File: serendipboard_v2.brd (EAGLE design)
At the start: 34.3 x 48.3 mm, 85 parts, among them IC1 TP4056, IC2 DW01A, IC3 DS3231/SO, J4 USB3076-XX-X_REVC, Q1 FS8205A, Q2 MMBT2222ALT1G, Q3 RUC002N05HZGT116, Q4 DMG3415U, Q5 MMBT2222ALT1G, Q7 RUC002N05HZGT116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

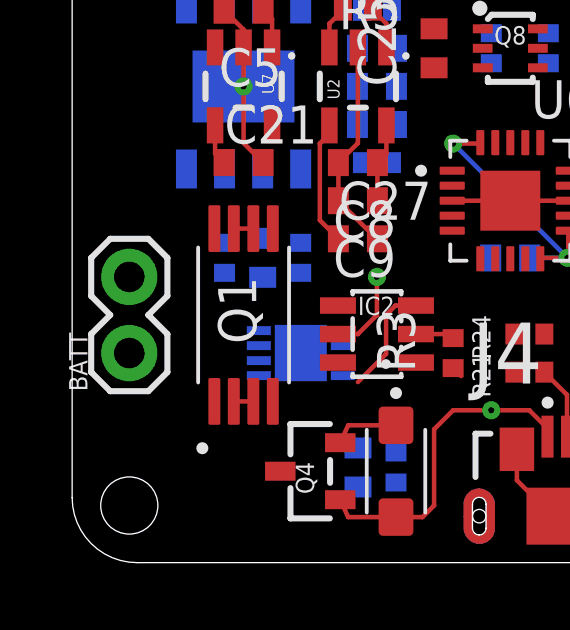
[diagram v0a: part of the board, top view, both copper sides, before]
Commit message: Update serendipboard_v2.brd
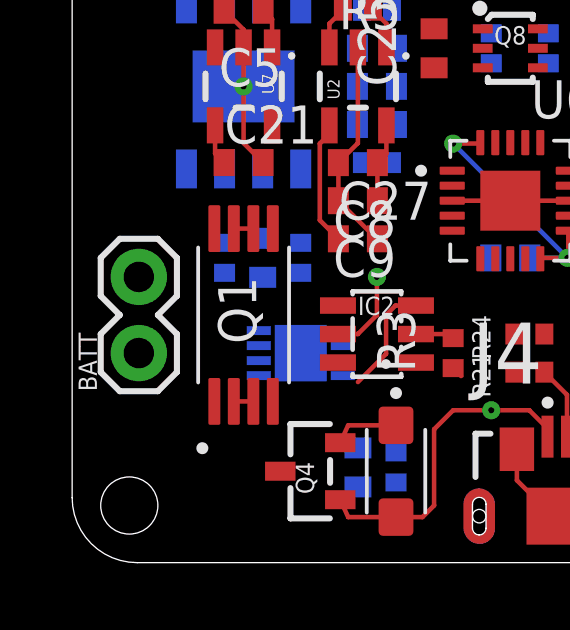
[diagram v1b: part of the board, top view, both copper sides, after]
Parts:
- moved BATT 0.32 mm to (2.22, 6.99)
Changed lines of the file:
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@@
 <attribute name="WEBLINK" value="https://www.mouser.com/ProductDetail/Microchip-Technology-Micrel/MIC5219-33YM5-TR?qs=U6T8BxXiZAWojkIJMtSJlw%3D%3D" x="-80.645" y="113.665" size="1.778" layer="27" rot="R180" display="off"/>
 </element>
-<element name="BATT" library="SparkFun-Connectors" package="1X02" value="" x="1.905" y="6.985" smashed="yes" rot="R90">
-<attribute name="NAME" x="0.508" y="5.715" size="0.6096" layer="25" font="vector" ratio="20" rot="R90"/>
-<attribute name="VALUE" x="3.937" y="5.715" size="0.6096" layer="27" font="vector" ratio="20" rot="R90"/>
+<element name="BATT" library="SparkFun-Connectors" package="1X02" value="" x="2.2225" y="6.985" smashed="yes" rot="R90">
+<attribute name="NAME" x="0.8255" y="5.715" size="0.6096" layer="25" font="vector" ratio="20" rot="R90"/>
+<attribute name="VALUE" x="4.2545" y="5.715" size="0.6096" layer="27" font="vector" ratio="20" rot="R90"/>
 </element>
 </elements>
@@
 <wire x1="6.04" y1="5.375" x2="5.39" y2="5.375" width="0.1524" layer="1"/>
 <contactref element="BATT" pad="1"/>
-<wire x1="1.905" y1="6.985" x2="5.39" y2="5.375" width="0" layer="19" extent="1-1"/>
+<wire x1="2.2225" y1="6.985" x2="5.39" y2="5.375" width="0" layer="19" extent="1-1"/>
 </signal>
 <signal name="N$4">
@@
 <wire x1="7.62" y1="13.125" x2="9.66" y2="13.335" width="0" layer="19" extent="16-16"/>
 <wire x1="5.08" y1="10.66" x2="7.62" y2="13.125" width="0" layer="19" extent="16-16"/>
-<wire x1="1.905" y1="9.525" x2="5.08" y2="10.66" width="0" layer="19" extent="16-16"/>
+<wire x1="2.2225" y1="9.525" x2="5.08" y2="10.66" width="0" layer="19" extent="16-16"/>
 <wire x1="6.9375" y1="3.048" x2="5.08" y2="10.66" width="0" layer="19" extent="1-16"/>
 </signal>

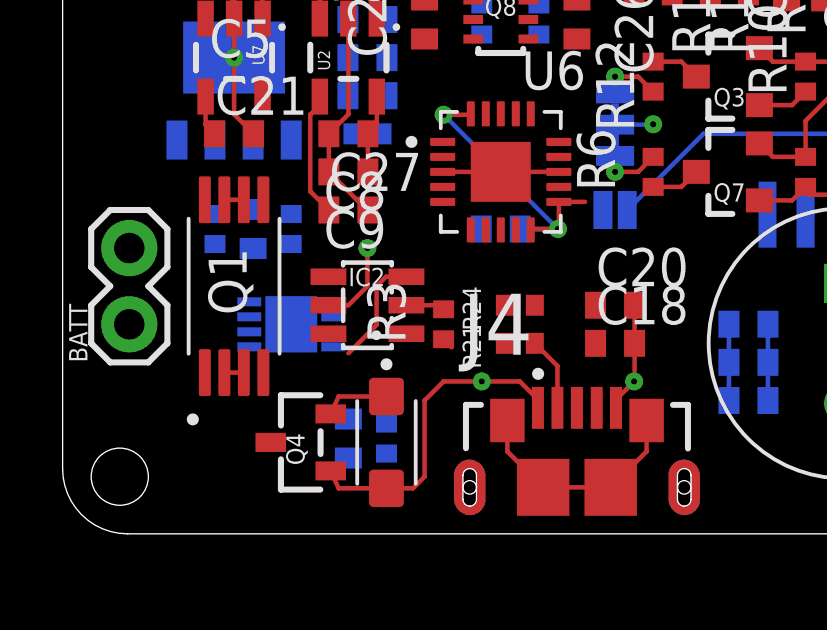
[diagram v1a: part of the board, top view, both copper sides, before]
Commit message: Update serendipboard_v2.brd
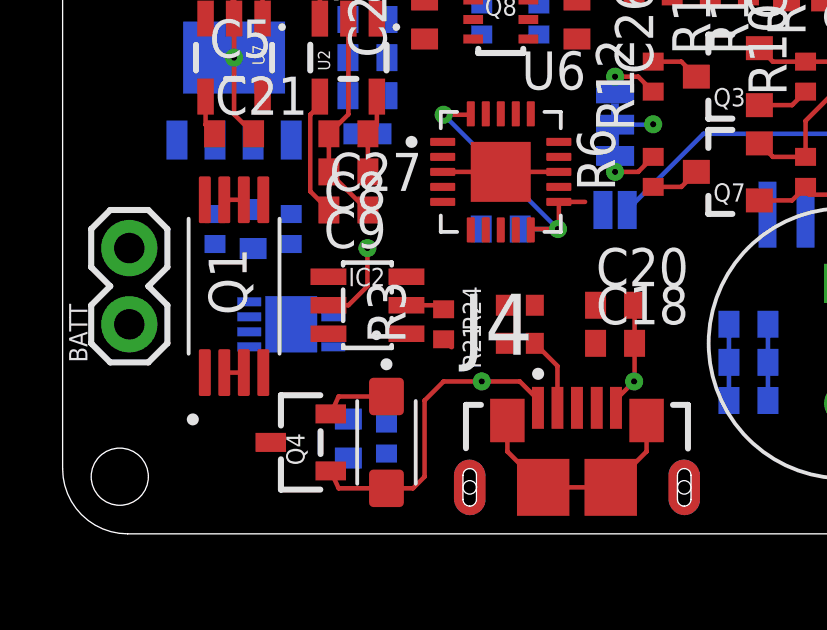
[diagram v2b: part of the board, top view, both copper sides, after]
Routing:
- net N$2: track 3.75 -> 0.00 mm
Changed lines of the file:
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@@
 <contactref element="Q1" pad="5"/>
 <contactref element="IC2" pad="3"/>
-<wire x1="9.525" y1="6.0198" x2="10.4648" y2="6.9596" width="0.1524" layer="1"/>
-<wire x1="10.4648" y1="6.9596" x2="10.4648" y2="8.255" width="0.1524" layer="1"/>
-<wire x1="10.4648" y1="8.255" x2="10.7798" y2="8.57" width="0.1524" layer="1"/>
-<wire x1="10.7798" y1="8.57" x2="11.46" y2="8.57" width="0.1524" layer="1"/>
-<wire x1="11.46" y1="8.57" x2="6.69" y2="11.135" width="0" layer="19" extent="1-1"/>
+<wire x1="6.69" y1="11.135" x2="11.46" y2="8.57" width="0" layer="19" extent="1-1"/>
 </signal>
 <signal name="N$5">

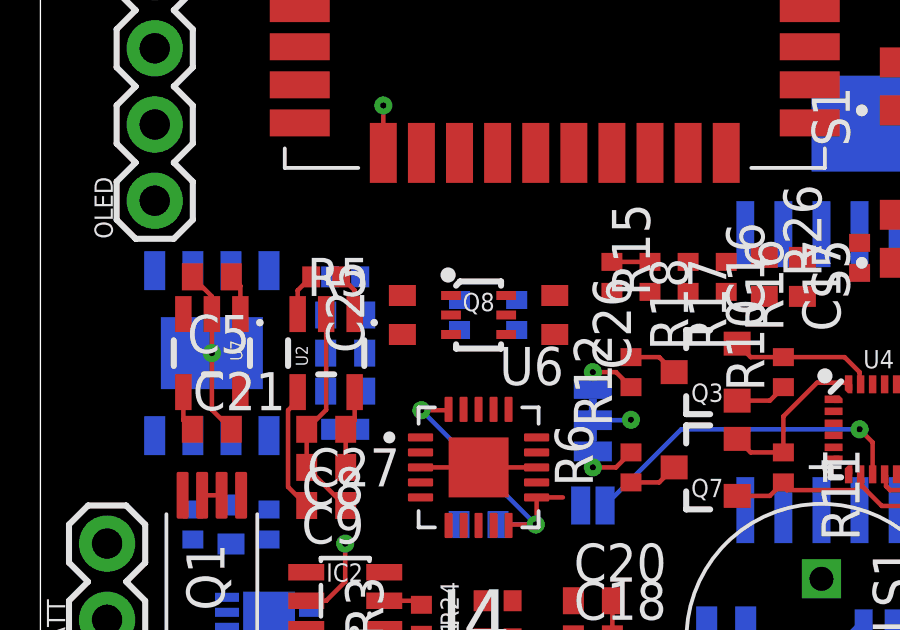
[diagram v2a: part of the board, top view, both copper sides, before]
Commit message: Update serendipboard_v2.brd
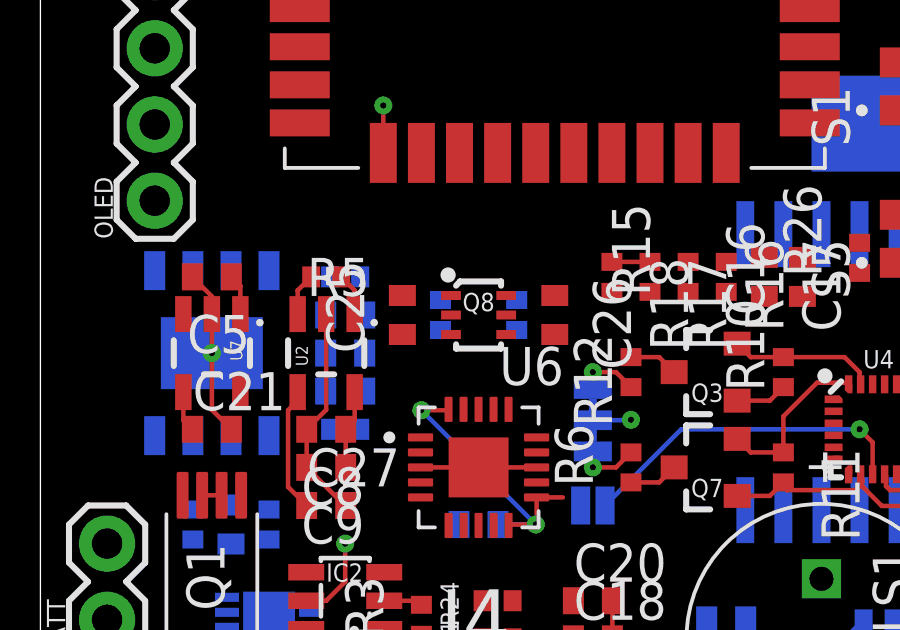
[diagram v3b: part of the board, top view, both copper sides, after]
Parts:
- moved R23 0.63 mm to (13.3, 17.1)
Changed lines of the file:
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@@
 </layers>
 <board>
-<fusionsync huburn="a.YnVzaW5lc3M6aG90bWFpbDIyNTY5Mg" projecturn="a.YnVzaW5lc3M6aG90bWFpbDIyNTY5MiNEMjAyMTAyMjYzODcwODA0ODE" f3durn="urn:adsk.wipprod:dm.lineage:5p1CPkeoRTeQBctxtFipzA" pcbguid="" lastpulledtime="" lastsyncedchangeguid="" latestrevisionid="0848454d-5bbb-43fb-8d8e-27c1f2ded824" lastsyncedrevisionid="0848454d-5bbb-43fb-8d8e-27c1f2ded824" lastboardhashguid="b401df1f-909b-11eb-b8ce-9c009d1c97d0" lastpushedtime="2021-03-17T16:29:33Z" linktopcb3d="false"/>
+<fusionsync huburn="a.YnVzaW5lc3M6aG90bWFpbDIyNTY5Mg" projecturn="a.YnVzaW5lc3M6aG90bWFpbDIyNTY5MiNEMjAyMTAyMjYzODcwODA0ODE" f3durn="urn:adsk.wipprod:dm.lineage:5p1CPkeoRTeQBctxtFipzA" pcbguid="" lastpulledtime="" lastsyncedchangeguid="" latestrevisionid="0848454d-5bbb-43fb-8d8e-27c1f2ded824" lastsyncedrevisionid="0848454d-5bbb-43fb-8d8e-27c1f2ded824" lastboardhashguid="b401df1f-909b-11eb-b8ce-9c009d1c97d0" lastpushedtime="2021-03-17T16:29:33Z" linktopcb3d="true"/>
 <fusionteam huburn="a.YnVzaW5lc3M6aG90bWFpbDIyNTY5Mg" projecturn="a.YnVzaW5lc3M6aG90bWFpbDIyNTY5MiNEMjAyMTAyMjYzODcwODA0ODE" folderUrn="urn:adsk.wipprod:fs.folder:co.dUA13uBtTS2Ov44EvO0svw" urn="urn:adsk.wipprod:dm.lineage:Zp6-x7SYSPeZgPEikwpQaw"  versionUrn="urn:adsk.wipprod:fs.file:vf.Zp6-x7SYSPeZgPEikwpQaw?version=1" camFileUrn="" camFileVersionUrn="" lastpublishedchangeguid="f1674931-6e59-d979-c39e-c9ae2950564c"/>
 <plain>
@@
 <attribute name="VALUE" x="18.415" y="17.78" size="1.27" layer="28" rot="MR270"/>
 </element>
-<element name="R23" library="rcl" library_urn="urn:adsk.eagle:library:334" package="R0402" package3d_urn="urn:adsk.eagle:package:23547/3" value="10k" x="13.97" y="17.145" smashed="yes" rot="MR270">
-<attribute name="NAME" x="12.7" y="19.05" size="1.27" layer="26" rot="MR90"/>
-<attribute name="POPULARITY" value="34" x="105.41" y="-5.715" size="1.778" layer="28" rot="MR270" display="off"/>
-<attribute name="SPICEPREFIX" value="R" x="105.41" y="-5.715" size="1.778" layer="28" rot="MR270" display="off"/>
-<attribute name="VALUE" x="16.51" y="17.78" size="1.27" layer="28" rot="MR270"/>
+<element name="R23" library="rcl" library_urn="urn:adsk.eagle:library:334" package="R0402" package3d_urn="urn:adsk.eagle:package:23547/3" value="10k" x="13.335" y="17.145" smashed="yes" rot="MR270">
+<attribute name="NAME" x="12.065" y="19.05" size="1.27" layer="26" rot="MR90"/>
+<attribute name="POPULARITY" value="34" x="104.775" y="-5.715" size="1.778" layer="28" rot="MR270" display="off"/>
+<attribute name="SPICEPREFIX" value="R" x="104.775" y="-5.715" size="1.778" layer="28" rot="MR270" display="off"/>
+<attribute name="VALUE" x="15.875" y="17.78" size="1.27" layer="28" rot="MR270"/>
 </element>
 <element name="R24" library="rcl" library_urn="urn:adsk.eagle:library:334" package="R0402" package3d_urn="urn:adsk.eagle:package:23547/3" value="27" x="15.24" y="7.62" smashed="yes" rot="R180">
@@
 <contactref element="R23" pad="2"/>
 <contactref element="Q8" pad="2"/>
-<wire x1="13.685" y1="17.145" x2="13.97" y2="16.645" width="0" layer="19" extent="1-16"/>
+<wire x1="13.685" y1="17.145" x2="13.335" y2="16.645" width="0" layer="19" extent="1-16"/>
 </signal>
 <signal name="EN">
@@
 <contactref element="Q8" pad="4"/>
 <contactref element="U6" pad="19"/>
-<wire x1="13.97" y1="17.645" x2="15.525" y2="16.495" width="0" layer="19" extent="1-16"/>
+<wire x1="13.335" y1="17.645" x2="15.525" y2="16.495" width="0" layer="19" extent="1-16"/>
 <wire x1="14.105" y1="14" x2="15.525" y2="16.495" width="0" layer="19" extent="1-1"/>
 </signal>

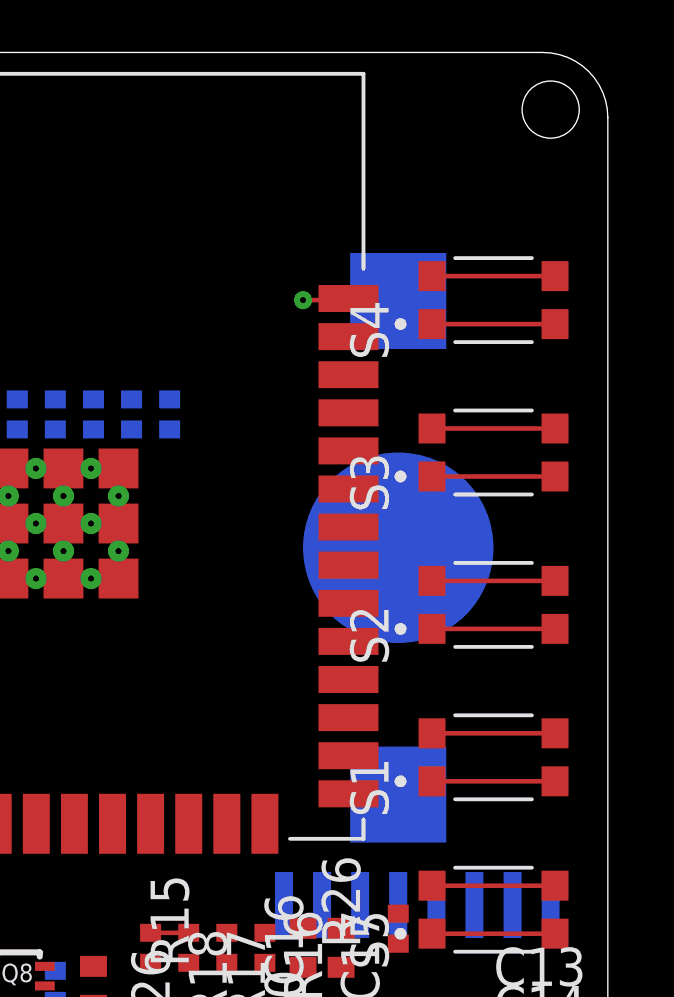
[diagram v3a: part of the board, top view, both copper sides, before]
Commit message: Update serendipboard_v2.brd
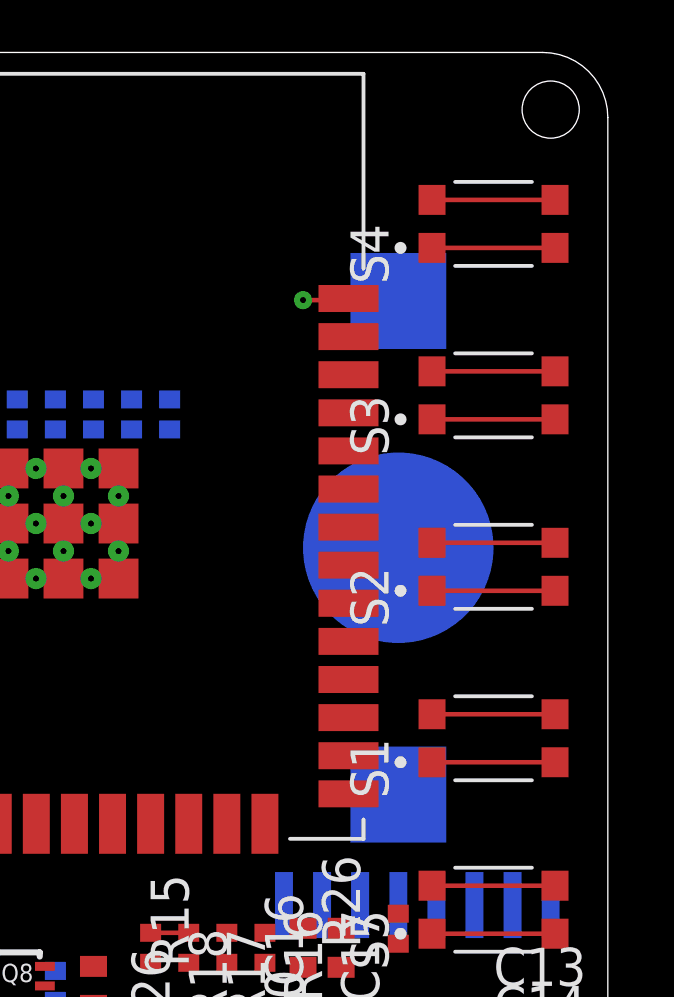
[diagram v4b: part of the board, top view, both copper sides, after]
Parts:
- moved S4 2.54 mm to (30.5, 42.5)
- moved S3 1.91 mm to (30.5, 36.8)
- moved S2 1.27 mm to (30.5, 31.1)
- moved S1 0.63 mm to (30.5, 25.4)

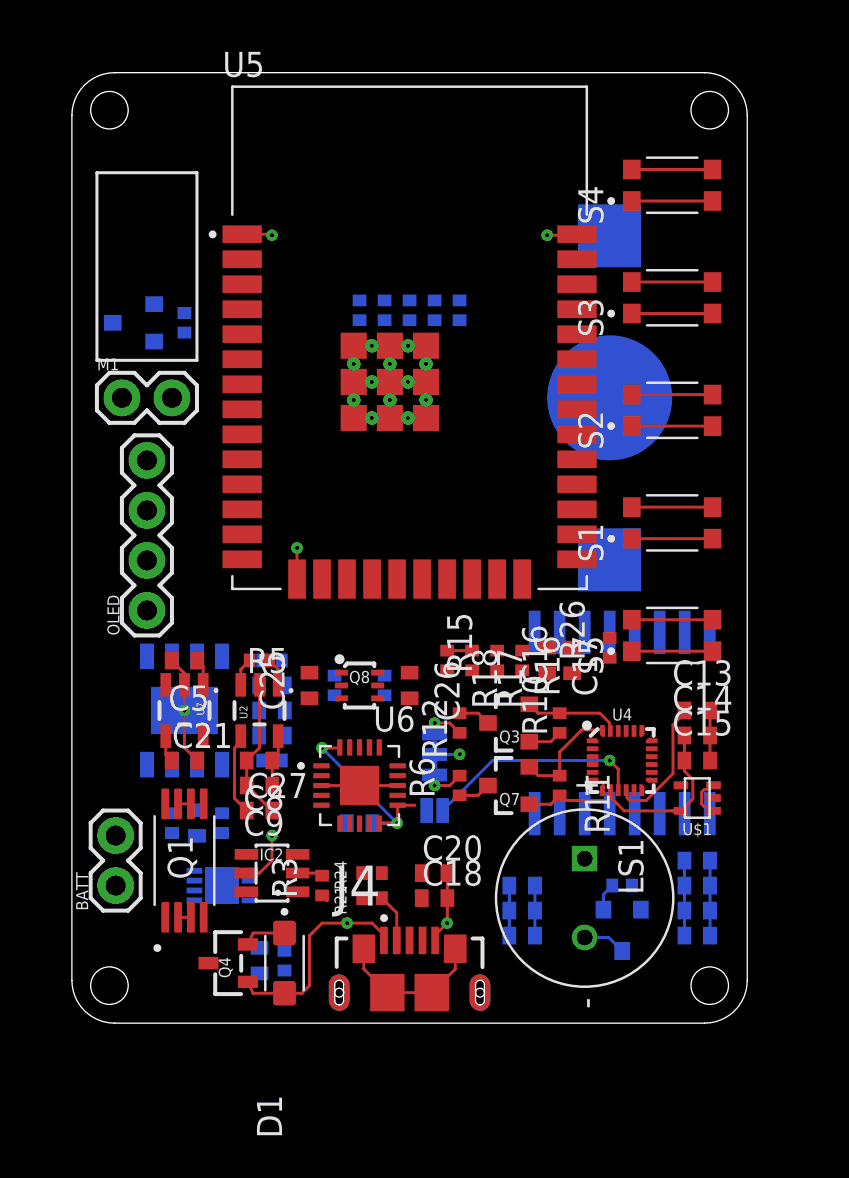
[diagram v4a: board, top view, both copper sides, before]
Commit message: Update serendipboard_v2.brd
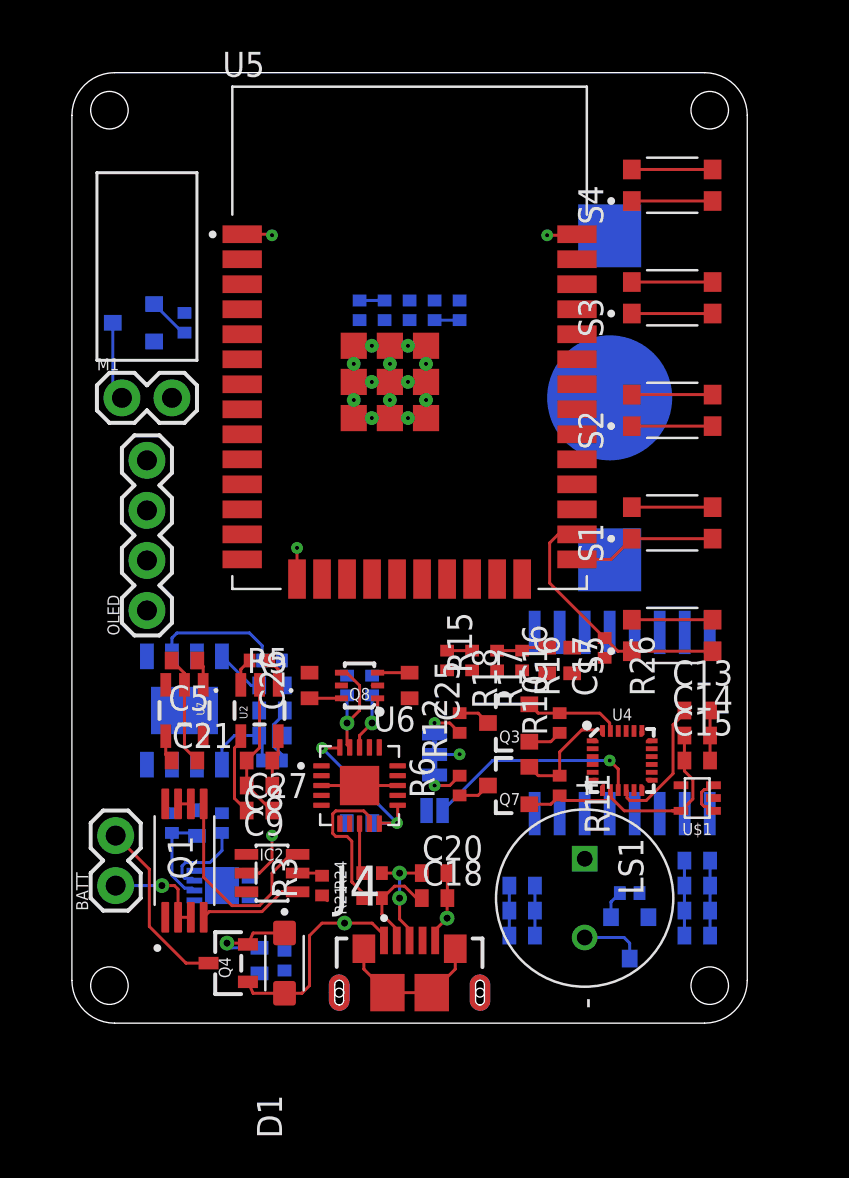
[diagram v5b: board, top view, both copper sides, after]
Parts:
- moved C25 5.08 mm to (17.1, 17.1), turned to 270 degrees
- moved C26 5.08 mm to (12.1, 17.1), turned to 90 degrees
- moved R22 0.63 mm to (15.2, 17.1)
- moved R23 0.63 mm to (14.0, 17.1), turned to 90 degrees
- moved Q2 0.54 mm to (28.3, 4.38)
- moved R14 0.54 mm to (28.3, 6.60)
- moved R26 0.25 mm to (27.1, 19.1), turned to 270 degrees
- turned Q8 to 90 degrees
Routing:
- net VBAT: track 0.00 -> 13.4 mm
- net N$2: track 0.00 -> 10.8 mm
- net PWR: track 4.10 -> 13.3 mm
- net N$20: track 0.00 -> 7.64 mm
- net N$1: track 0.00 -> 6.64 mm
- net RTS: track 0.00 -> 6.06 mm, vias 0 -> 1
- net N$21: track 0.00 -> 5.66 mm, vias 0 -> 2
- net N$4: track 0.00 -> 5.31 mm
- net N$7: track 0.00 -> 4.95 mm
- net IO0: track 4.10 -> 8.94 mm
- net B-: track 0.65 -> 5.32 mm, vias 0 -> 1
- net N$6: track 0.00 -> 4.47 mm
- net DTR: track 0.00 -> 4.28 mm, vias 0 -> 1
- net N$17: track 0.00 -> 4.00 mm
- net N$3: track 2.83 -> 5.79 mm
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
